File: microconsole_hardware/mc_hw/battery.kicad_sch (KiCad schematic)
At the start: 22 parts, among them J1 USB_C_Receptacle_USB2.0_16P, Q1 DMP2035U-7, Q2 DMP2035U-7, SW19 SPDT_Slide_PTH_11.6x4.0mm, U1 MCP73833-FCI/UN, U2 S2B-PH-K-S

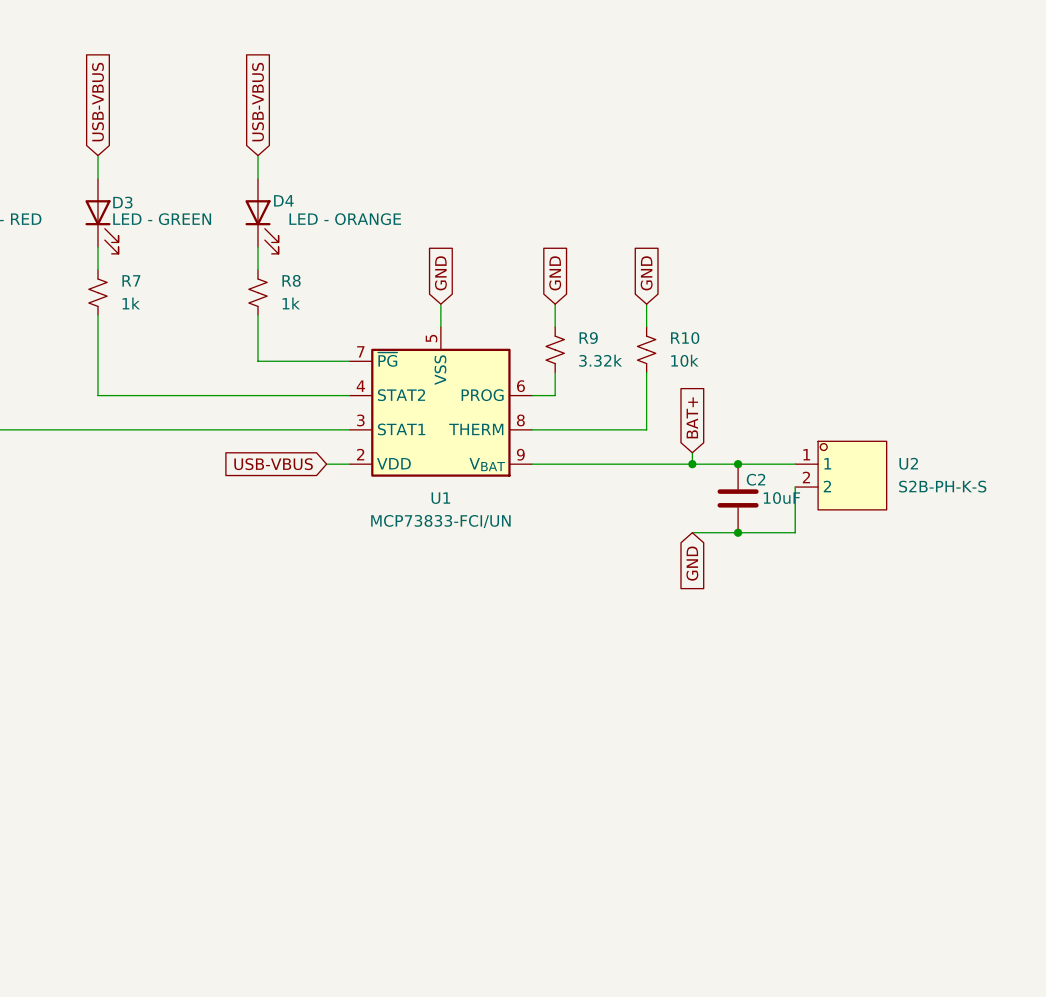
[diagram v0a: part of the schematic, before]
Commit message: add battery sense and thermistor
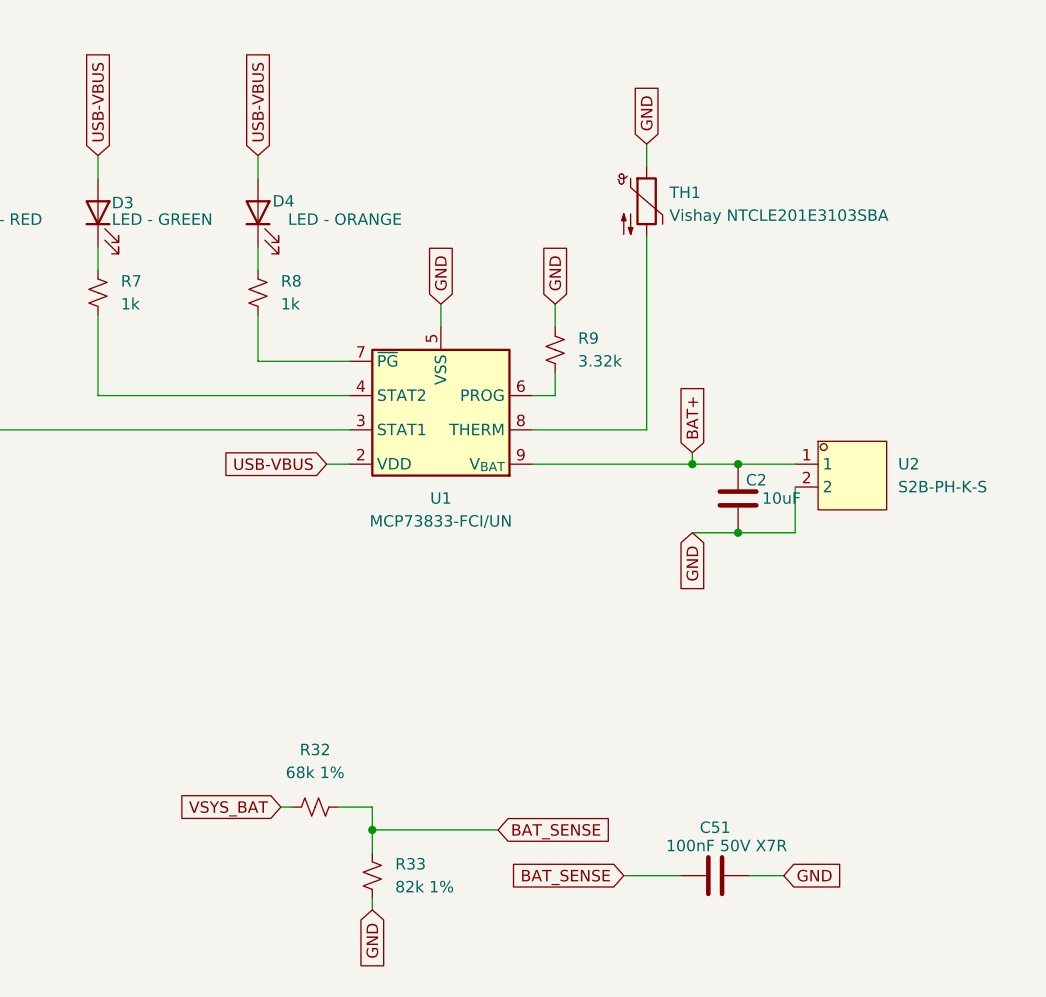
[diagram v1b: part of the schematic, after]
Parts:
- removed R10: 10k, PCM_SparkFun-Resistor:R_0603_1608Metric, symbol PCM_SparkFun-Resistor:0.47_0603
- added C51: 100nF 50V X7R, project_parts:C_0805_2012Metric_KEMET_IPC-B, symbol project_parts:C0805C104K5RAC7210
- added R32: 68k 1%, PCM_SparkFun-Resistor:R_0603_1608Metric, symbol PCM_SparkFun-Resistor:0.47_0603
- added R33: 82k 1%, PCM_SparkFun-Resistor:R_0603_1608Metric, symbol PCM_SparkFun-Resistor:0.47_0603
- added TH1: Vishay NTCLE201E3103SBA, Connector_PinHeader_2.54mm:PinHeader_1x02_P2.54mm_Vertical, symbol Device:Thermistor_NTC
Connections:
- net GND: now also C51.1, R33.1, TH1.1
- net VSYS_BAT: now also R32.2
- net at U1.8 (THERM): now also TH1.2
- new net BAT_SENSE: C51.2, R32.1, R33.2

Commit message: Fix usb
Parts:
- removed J1: USB_C_Receptacle_USB2.0_16P, Connector_USB:USB_C_Receptacle_GCT_USB4135-GF-A_6P_TopMnt_Horizontal, symbol project_parts:USB_C_Receptacle_USB2.0_16P
- added J2: USB_C_Receptacle, Connector_USB:USB_C_Receptacle_HCTL_HC-TYPE-C-16P-01A, symbol Connector:USB_C_Receptacle_PowerOnly_24P
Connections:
- net GND: now also J2.A1 (GND), J2.A12 (GND), J2.B1 (GND), J2.B12 (GND), J2.SH (SHIELD)
- net VDD: now also J2.A4 (VBUS), J2.A9 (VBUS), J2.B4 (VBUS), J2.B9 (VBUS)
- net at R3.1: now also J2.A5 (CC1)
- net at R4.2: now also J2.B5 (CC2)
- no-connect marks 7 -> 1
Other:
- moved on the sheet: C1, R3, R4

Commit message: completely fix up board and schematic
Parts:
- D2, D3, D4: footprint (none) -> LED_SMD:LED_0603_1608Metric_Pad1.05x0.95mm_HandSolder
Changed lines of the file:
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@@
 			)
 		)
-		(property "Footprint" ""
+		(property "Footprint" "LED_SMD:LED_0603_1608Metric_Pad1.05x0.95mm_HandSolder"
 			(at 191.77 44.45 0)
 			(hide yes)
@@
 			)
 		)
-		(property "Footprint" ""
+		(property "Footprint" "LED_SMD:LED_0603_1608Metric_Pad1.05x0.95mm_HandSolder"
 			(at 157.48 44.45 0)
 			(hide yes)
@@
 			)
 		)
-		(property "Footprint" ""
+		(property "Footprint" "LED_SMD:LED_0603_1608Metric_Pad1.05x0.95mm_HandSolder"
 			(at 173.99 44.45 0)
 			(hide yes)

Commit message: fixup things
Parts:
- C1, C2: footprint (none) -> project_parts:C_0805_2012Metric_KEMET_IPC-B
- U1: symbol PCM_SparkFun-IC-Power:MCP73833 -> project_parts:MCP73833
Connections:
- net BAT+: no longer U1.10 (V_{BAT})
- net VDD renamed USB-VBUS
- net USB-VBUS: no longer U1.1 (VDD)
- no-connect marks 1 -> 3
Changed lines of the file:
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@@
-	)
-	(junction
-		(at 193.04 72.39)
-		(diameter 0)
-		(color 0 0 0 0)
 	)
 	(junction
@@
 	)
 	(junction
+		(at 53.34 39.37)
+		(diameter 0)
+		(color 0 0 0 0)
+	)
+	(junction
 		(at 245.11 80.01)
 		(diameter 0)
@@
 	)
 	(no_connect
+		(at 213.36 76.2)
+	)
+	(no_connect
+		(at 210.82 76.2)
+	)
+	(no_connect
 		(at 109.22 50.8)
 	)
@@
 	(wire
 		(pts
+			(xy 177.8 72.39) (xy 187.96 72.39)
+		)
+		(stroke
+			(width 0)
+			(type default)
+		)
+	)
+	(wire
+		(pts
+			(xy 200.66 72.39) (xy 201.93 72.39)
+		)
+		(stroke
+			(width 0)
+			(type default)
+		)
+	)
+	(wire
+		(pts
 			(xy 173.99 48.26) (xy 173.99 50.8)
 		)
@@
 	(wire
 		(pts
+			(xy 222.25 72.39) (xy 251.46 72.39)
+		)
+		(stroke
+			(width 0)
+			(type default)
+		)
+	)
+	(wire
+		(pts
 			(xy 240.03 80.01) (xy 245.11 80.01)
 		)
@@
 	(wire
 		(pts
-			(xy 193.04 72.39) (xy 201.93 72.39)
-		)
-		(stroke
-			(width 0)
-			(type default)
-		)
-	)
-	(wire
-		(pts
 			(xy 204.47 121.92) (xy 204.47 120.65)
 		)
@@
 	(wire
 		(pts
-			(xy 43.18 39.37) (xy 72.39 39.37)
+			(xy 43.18 39.37) (xy 53.34 39.37)
 		)
 		(stroke
@@
 	(wire
 		(pts
+			(xy 53.34 39.37) (xy 72.39 39.37)
+		)
+		(stroke
+			(width 0)
+			(type default)
+		)
+	)
+	(wire
+		(pts
 			(xy 48.26 52.07) (xy 43.18 52.07)
 		)
@@
 	(wire
 		(pts
-			(xy 222.25 72.39) (xy 251.46 72.39)
-		)
-		(stroke
-			(width 0)
-			(type default)
-		)
-	)
-	(wire
-		(pts
 			(xy 119.38 116.84) (xy 119.38 118.11)
 		)
@@
 	(wire
 		(pts
-			(xy 187.96 72.39) (xy 193.04 72.39)
-		)
-		(stroke
-			(width 0)
-			(type default)
-		)
-	)
-	(wire
-		(pts
 			(xy 55.88 52.07) (xy 59.69 52.07)
 		)
@@
 		)
 	)
+	(global_label "VDD"
+		(shape input)
+		(at 187.96 72.39 0)
+		(fields_autoplaced yes)
+		(effects
+			(font
+				(size 1.27 1.27)
+			)
+			(justify left)
+		)
+		(property "Intersheetrefs" "${INTERSHEET_REFS}"
+			(at 194.5738 72.39 0)
+			(hide yes)
+			(show_name no)
+			(do_not_autoplace no)
+			(effects
+				(font
+					(size 1.27 1.27)
+				)
+				(justify left)
+			)
+		)
+	)
 	(global_label "USB-VBUS"
 		(shape input)
@@
 	(global_label "USB-VBUS"
 		(shape input)
-		(at 187.96 72.39 180)
+		(at 177.8 72.39 180)
 		(fields_autoplaced yes)
 		(effects
@@
 		)
 		(property "Intersheetrefs" "${INTERSHEET_REFS}"
-			(at 174.6938 72.39 0)
+			(at 164.5338 72.39 0)
 			(hide yes)
 			(show_name no)
@@
 				)
 				(justify left)
+			)
+		)
+	)
+	(global_label "VDD"
+		(shape input)
+		(at 200.66 72.39 180)
+		(fields_autoplaced yes)
+		(effects
+			(font
+				(size 1.27 1.27)
+			)
+			(justify right)
+		)
+		(property "Intersheetrefs" "${INTERSHEET_REFS}"
+			(at 194.0462 72.39 0)
+			(hide yes)
+			(show_name no)
+			(do_not_autoplace no)
+			(effects
+				(font
+					(size 1.27 1.27)
+				)
+				(justify right)
 			)
 		)
@@
 	)
 	(symbol
+		(lib_id "power:PWR_FLAG")
+		(at 53.34 39.37 0)
+		(unit 1)
+		(body_style 1)
+		(exclude_from_sim no)
+		(in_bom yes)
+		(on_board yes)
+		(in_pos_files yes)
+		(dnp no)
+		(fields_autoplaced yes)
+		(property "Reference" "#FLG02"
+			(at 53.34 37.465 0)
+			(hide yes)
+			(show_name no)
+			(do_not_autoplace no)
+			(effects
+				(font
+					(size 1.27 1.27)
+				)
+			)
+		)
+		(property "Value" "PWR_FLAG"
+			(at 53.34 34.29 0)
+			(show_name no)
+			(do_not_autoplace no)
+			(effects
+				(font
+					(size 1.27 1.27)
+				)
+			)
+		)
+		(property "Footprint" ""
+			(at 53.34 39.37 0)
+			(hide yes)
+			(show_name no)
+			(do_not_autoplace no)
+			(effects
+				(font
+					(size 1.27 1.27)
+				)
+			)
+		)
+		(property "Datasheet" ""
+			(at 53.34 39.37 0)
+			(hide yes)
+			(show_name no)
+			(do_not_autoplace no)
+			(effects
+				(font
+					(size 1.27 1.27)
+				)
+			)
+		)
+		(property "Description" "Special symbol for telling ERC where power comes from"
+			(at 53.34 39.37 0)
+			(hide yes)
+			(show_name no)
+			(do_not_autoplace no)
+			(effects
+				(font
+					(size 1.27 1.27)
+				)
+			)
+		)
+		(pin "1"
+		)
+		(instances
+			(project "top"
+				(path "/3433afdc-e53a-48bd-a2b1-9fdee73e8b40/2e88eeda-748f-4d75-b88b-5acda3278369"
+					(reference "#FLG02")
+					(unit 1)
+				)
+			)
+		)
+	)
+	(symbol
 		(lib_id "project_parts:C0805C104K5RAC7210")
 		(at 242.57 118.11 270)
@@
 			)
 		)
-		(property "Footprint" ""
+		(property "Footprint" "project_parts:C_0805_2012Metric_KEMET_IPC-B"
 			(at 66.3448 41.91 0)
 			(hide yes)
@@
 	)
 	(symbol
-		(lib_id "PCM_SparkFun-IC-Power:MCP73833")
+		(lib_id "project_parts:MCP73833")
 		(at 212.09 63.5 180)
 		(unit 1)
@@
 		(in_pos_files yes)
 		(dnp no)
-		(fields_autoplaced yes)
 		(property "Reference" "U1"
-			(at 212.09 76.2 0)
-			(show_name no)
-			(do_not_autoplace no)
-			(effects
-				(font
-					(size 1.27 1.27)
-				)
+			(at 205.74 75.184 0)
+			(show_name no)
+			(do_not_autoplace no)
+			(effects
+				(font
+					(size 1.27 1.27)
+				)
+				(justify right)
 			)
 		)
 		(property "Value" "MCP73833-FCI/UN"
-			(at 212.09 78.74 0)
-			(show_name no)
-			(do_not_autoplace no)
-			(effects
-				(font
-					(size 1.27 1.27)
-				)
+			(at 191.516 77.724 0)
+			(show_name no)
+			(do_not_autoplace no)
+			(effects
+				(font
+					(size 1.27 1.27)
+				)
+				(justify right)
 			)
 		)
@@
 			)
 		)
-		(property "Footprint" ""
+		(property "Footprint" "project_parts:C_0805_2012Metric_KEMET_IPC-B"
 			(at 246.0752 80.01 0)
 			(hide yes)
@@
 					(unit 1)
 				)
-			)
-		)
-	)
-	(symbol
-		(lib_id "power:PWR_FLAG")
-		(at 193.04 72.39 180)
-		(unit 1)
-		(body_style 1)
-		(exclude_from_sim no)
-		(in_bom yes)
-		(on_board yes)
-		(in_pos_files yes)
-		(dnp no)
-		(fields_autoplaced yes)
-		(property "Reference" "#FLG02"
-			(at 193.04 74.295 0)
-			(hide yes)
-			(show_name no)
-			(do_not_autoplace no)
-			(effects
-				(font
-					(size 1.27 1.27)
-				)
-			)
-		)
-		(property "Value" "PWR_FLAG"
-			(at 193.04 77.47 0)
-			(show_name no)
-			(do_not_autoplace no)
-			(effects
-				(font
-					(size 1.27 1.27)
-				)
-			)
-		)
-		(property "Footprint" ""
-			(at 193.04 72.39 0)
-			(hide yes)
-			(show_name no)
-			(do_not_autoplace no)
-			(effects
-				(font
-					(size 1.27 1.27)
-				)
-			)
-		)
-		(property "Datasheet" ""
-			(at 193.04 72.39 0)
-			(hide yes)
-			(show_name no)
-			(do_not_autoplace no)
-			(effects
-				(font
-					(size 1.27 1.27)
-				)
-			)
-		)
-		(property "Description" "Special symbol for telling ERC where power comes from"
-			(at 193.04 72.39 0)
-			(hide yes)
-			(show_name no)
-			(do_not_autoplace no)
-			(effects
-				(font
-					(size 1.27 1.27)
-				)
-			)
-		)
-		(pin "1"
-		)
-		(instances
-			(project "top"
-				(path "/3433afdc-e53a-48bd-a2b1-9fdee73e8b40/2e88eeda-748f-4d75-b88b-5acda3278369"
-					(reference "#FLG02")
-					(unit 1)
-				)

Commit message: fix2
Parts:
- D1: footprint (none) -> Diode_SMD:D_SOD-123W
- TH1: symbol Device:Thermistor_NTC -> project_parts:Thermistor_NTC_Wired
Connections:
- net BAT+: now also U1.10 (V_{BAT})
- net USB-VBUS: now also U1.1 (VDD)
- no-connect marks 3 -> 1
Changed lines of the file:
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@@
 	)
 	(junction
+		(at 200.66 72.39)
+		(diameter 0)
+		(color 0 0 0 0)
+	)
+	(junction
 		(at 240.03 72.39)
 		(diameter 0)
@@
 	)
 	(no_connect
-		(at 213.36 76.2)
-	)
-	(no_connect
-		(at 210.82 76.2)
-	)
-	(no_connect
 		(at 109.22 50.8)
 	)
@@
 	(wire
 		(pts
-			(xy 177.8 72.39) (xy 187.96 72.39)
+			(xy 195.58 72.39) (xy 200.66 72.39)
 		)
 		(stroke
@@
 	(wire
 		(pts
+			(xy 240.03 76.2) (xy 240.03 72.39)
+		)
+		(stroke
+			(width 0)
+			(type default)
+		)
+	)
+	(wire
+		(pts
 			(xy 222.25 68.58) (xy 234.95 68.58)
 		)
@@
 	(wire
 		(pts
+			(xy 213.36 76.2) (xy 240.03 76.2)
+		)
+		(stroke
+			(width 0)
+			(type default)
+		)
+	)
+	(wire
+		(pts
 			(xy 119.38 116.84) (xy 119.38 118.11)
 		)
@@
 	(wire
 		(pts
+			(xy 200.66 76.2) (xy 200.66 72.39)
+		)
+		(stroke
+			(width 0)
+			(type default)
+		)
+	)
+	(wire
+		(pts
 			(xy 173.99 38.1) (xy 173.99 40.64)
 		)
@@
 	(wire
 		(pts
+			(xy 210.82 76.2) (xy 200.66 76.2)
+		)
+		(stroke
+			(width 0)
+			(type default)
+		)
+	)
+	(wire
+		(pts
 			(xy 234.95 36.83) (xy 234.95 39.37)
 		)
@@
 		)
 	)
-	(global_label "VDD"
-		(shape input)
-		(at 187.96 72.39 0)
-		(fields_autoplaced yes)
-		(effects
-			(font
-				(size 1.27 1.27)
-			)
-			(justify left)
-		)
-		(property "Intersheetrefs" "${INTERSHEET_REFS}"
-			(at 194.5738 72.39 0)
-			(hide yes)
-			(show_name no)
-			(do_not_autoplace no)
-			(effects
-				(font
-					(size 1.27 1.27)
-				)
-				(justify left)
-			)
-		)
-	)
 	(global_label "USB-VBUS"
 		(shape input)
@@
 	(global_label "USB-VBUS"
 		(shape input)
-		(at 177.8 72.39 180)
+		(at 195.58 72.39 180)
 		(fields_autoplaced yes)
 		(effects
@@
 		)
 		(property "Intersheetrefs" "${INTERSHEET_REFS}"
-			(at 164.5338 72.39 0)
+			(at 182.3138 72.39 0)
 			(hide yes)
 			(show_name no)
@@
 		)
 	)
-	(global_label "VDD"
-		(shape input)
-		(at 200.66 72.39 180)
-		(fields_autoplaced yes)
-		(effects
-			(font
-				(size 1.27 1.27)
-			)
-			(justify right)
-		)
-		(property "Intersheetrefs" "${INTERSHEET_REFS}"
-			(at 194.0462 72.39 0)
-			(hide yes)
-			(show_name no)
-			(do_not_autoplace no)
-			(effects
-				(font
-					(size 1.27 1.27)
-				)
-				(justify right)
-			)
-		)
-	)
 	(global_label "GND"
 		(shape input)
@@
 			)
 		)
-		(property "Footprint" ""
+		(property "Footprint" "Diode_SMD:D_SOD-123W"
 			(at 120.65 38.1 0)
 			(hide yes)
@@
 			)
 		)
-		(property "Datasheet" ""
+		(property "Datasheet" "https://assets.nexperia.com/documents/data-sheet/PMEG40T30ER.pdf"
 			(at 120.65 38.1 0)
 			(hide yes)
@@
 	)
 	(symbol
-		(lib_id "Device:Thermistor_NTC")
+		(lib_id "project_parts:Thermistor_NTC_Wired")
 		(at 234.95 43.18 0)
 		(unit 1)

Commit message: fix up
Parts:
- D1: footprint Diode_SMD:D_SOD-123W -> Diode_SMD:Nexperia_CFP3_SOD-123W; symbol Device:D_Schottky -> project_parts:D_Schottky
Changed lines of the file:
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@@
 	)
 	(symbol
-		(lib_id "Device:D_Schottky")
+		(lib_id "project_parts:D_Schottky")
 		(at 120.65 38.1 180)
 		(unit 1)
@@
 			)
 		)
-		(property "Footprint" "Diode_SMD:D_SOD-123W"
+		(property "Footprint" "Diode_SMD:Nexperia_CFP3_SOD-123W"
 			(at 120.65 38.1 0)
 			(hide yes)
